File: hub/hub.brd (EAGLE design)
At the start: 31.8 x 25.4 mm, 5 parts

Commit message: closest you can get to Bailey's without getting your nose wet
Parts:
- moved Rπ 2.84 mm to (3.81, 19.1)
- moved C3 1.27 mm to (25.4, 20.3)
- moved XB24 1.27 mm to (7.62, 12.7)
- moved C4 1.27 mm to (27.9, 20.3)
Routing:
- net N$1: track 30.3 -> 29.2 mm
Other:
- board size 31.8 x 25.4 mm -> 29.5 x 26 mm
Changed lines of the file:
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@@
 <board>
 <plain>
-<wire x1="0" y1="0" x2="31.75" y2="0" width="0" layer="20"/>
-<wire x1="31.75" y1="0" x2="31.75" y2="25.4" width="0" layer="20"/>
-<wire x1="31.75" y1="25.4" x2="0" y2="25.4" width="0" layer="20"/>
-<wire x1="0" y1="25.4" x2="0" y2="0" width="0" layer="20"/>
+<wire x1="0" y1="0" x2="29.464" y2="0" width="0" layer="20"/>
+<wire x1="29.464" y1="0" x2="29.464" y2="26.035" width="0" layer="20"/>
+<wire x1="29.464" y1="26.035" x2="0" y2="26.035" width="0" layer="20"/>
+<wire x1="0" y1="26.035" x2="0" y2="0" width="0" layer="20"/>
 <text x="21.59" y="36.83" size="1.778" layer="51" ratio="15">Harold Cooper</text>
 <text x="20.32" y="12.7" size="1.778" layer="21" font="vector" ratio="15" align="center">Heat Seek
@@
 <elements>
 <element name="FRAME1" library="SparkFun-Aesthetics" package="CREATIVE_COMMONS" value="FRAME-LETTER" x="-6.35" y="36.83"/>
-<element name="Rπ" library="SparkFun-Connectors" package="2X5_NOSILK" value="M05X2NO_SILK" x="5.08" y="16.51" rot="MR0"/>
-<element name="XB24" library="hrldcpr" package="XBEE-1" value="XBEE-1XBEE-1" x="8.89" y="12.7" rot="R270"/>
-<element name="C3" library="SparkFun-Capacitors" package="0805" value="1µF" x="26.67" y="20.32" rot="R270"/>
-<element name="C4" library="SparkFun-Capacitors" package="0805" value="8.2pF" x="29.21" y="20.32" rot="R270"/>
+<element name="Rπ" library="SparkFun-Connectors" package="2X5_NOSILK" value="M05X2NO_SILK" x="3.81" y="19.05" rot="MR0"/>
+<element name="XB24" library="hrldcpr" package="XBEE-1" value="XBEE-1XBEE-1" x="7.62" y="12.7" rot="R270"/>
+<element name="C3" library="SparkFun-Capacitors" package="0805" value="1µF" x="25.4" y="20.32" rot="R270"/>
+<element name="C4" library="SparkFun-Capacitors" package="0805" value="8.2pF" x="27.94" y="20.32" rot="R270"/>
 </elements>
 <signals>
@@
 <polygon width="0.3048" layer="1" isolate="0.3048">
 <vertex x="0" y="0"/>
-<vertex x="0" y="25.4"/>
-<vertex x="30.48" y="25.4"/>
-<vertex x="30.48" y="0"/>
+<vertex x="0" y="26.035"/>
+<vertex x="29.464" y="26.035"/>
+<vertex x="29.464" y="0"/>
 </polygon>
 </signal>
@@
 <polygon width="0.3048" layer="16" isolate="0.3048">
 <vertex x="0" y="0"/>
-<vertex x="0" y="25.4"/>
-<vertex x="30.48" y="25.4"/>
-<vertex x="30.48" y="0"/>
+<vertex x="0" y="26.035"/>
+<vertex x="29.464" y="26.035"/>
+<vertex x="29.464" y="0"/>
 </polygon>
 <contactref element="Rπ" pad="1"/>
@@
 <contactref element="C4" pad="1"/>
 <contactref element="XB24" pad="1"/>
-<wire x1="26.67" y1="21.22" x2="29.21" y2="21.22" width="0.254" layer="1"/>
-<wire x1="28.89" y1="23.7" x2="28.89" y2="21.22" width="0.254" layer="1"/>
-<wire x1="28.89" y1="21.22" x2="29.21" y2="21.22" width="0.254" layer="1"/>
+<wire x1="25.4" y1="21.22" x2="27.94" y2="21.22" width="0.254" layer="1"/>
+<wire x1="27.62" y1="23.7" x2="27.62" y2="21.22" width="0.254" layer="1"/>
+<wire x1="27.62" y1="21.22" x2="27.94" y2="21.22" width="0.254" layer="1"/>
 </signal>
 <signal name="N$2">
 <contactref element="Rπ" pad="8"/>
 <contactref element="XB24" pad="3"/>
-<wire x1="3.81" y1="13.97" x2="1.27" y2="11.43" width="0.254" layer="1"/>
-<wire x1="1.27" y1="11.43" x2="3.81" y2="8.89" width="0.254" layer="1"/>
-<wire x1="3.81" y1="8.89" x2="10.08" y2="8.89" width="0.254" layer="1"/>
-<wire x1="10.08" y1="8.89" x2="24.89" y2="23.7" width="0.254" layer="1"/>
+<wire x1="2.54" y1="16.51" x2="1.143" y2="16.51" width="0.254" layer="1"/>
+<wire x1="1.143" y1="16.51" x2="1.143" y2="11.43" width="0.254" layer="1"/>
+<wire x1="23.62" y1="23.7" x2="11.35" y2="11.43" width="0.254" layer="1"/>
+<wire x1="11.35" y1="11.43" x2="1.143" y2="11.43" width="0.254" layer="1"/>
 </signal>
 <signal name="N$1">
 <contactref element="Rπ" pad="10"/>
 <contactref element="XB24" pad="2"/>
-<wire x1="3.81" y1="11.43" x2="6.35" y2="8.89" width="0.254" layer="16"/>
-<wire x1="6.35" y1="8.89" x2="12.08" y2="8.89" width="0.254" layer="16"/>
-<wire x1="12.08" y1="8.89" x2="26.89" y2="23.7" width="0.254" layer="16"/>
+<wire x1="2.54" y1="13.97" x2="5.08" y2="11.43" width="0.254" layer="16"/>
+<wire x1="13.35" y1="11.43" x2="25.62" y2="23.7" width="0.254" layer="16"/>
+<wire x1="5.08" y1="11.43" x2="13.35" y2="11.43" width="0.254" layer="16"/>
 </signal>
 </signals>

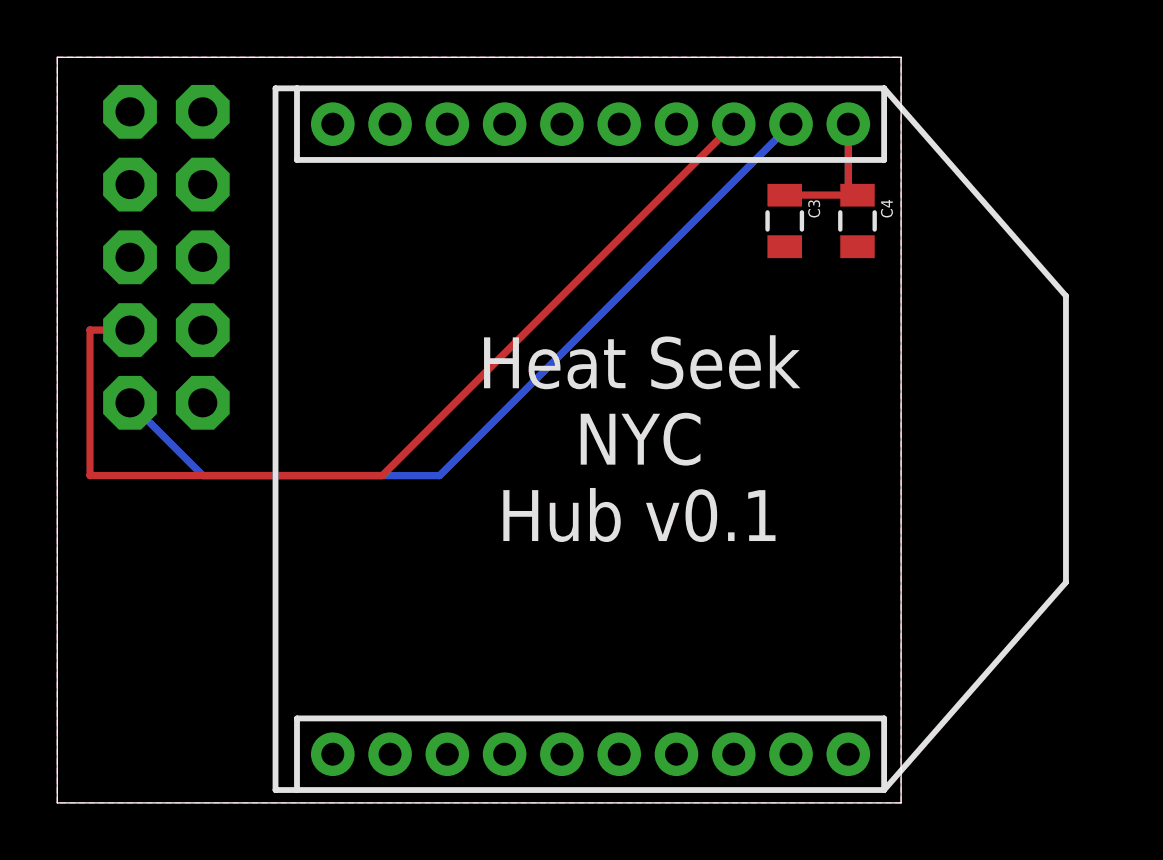
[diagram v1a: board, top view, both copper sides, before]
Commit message: use the largest header we can fit, for stability and to look cool?
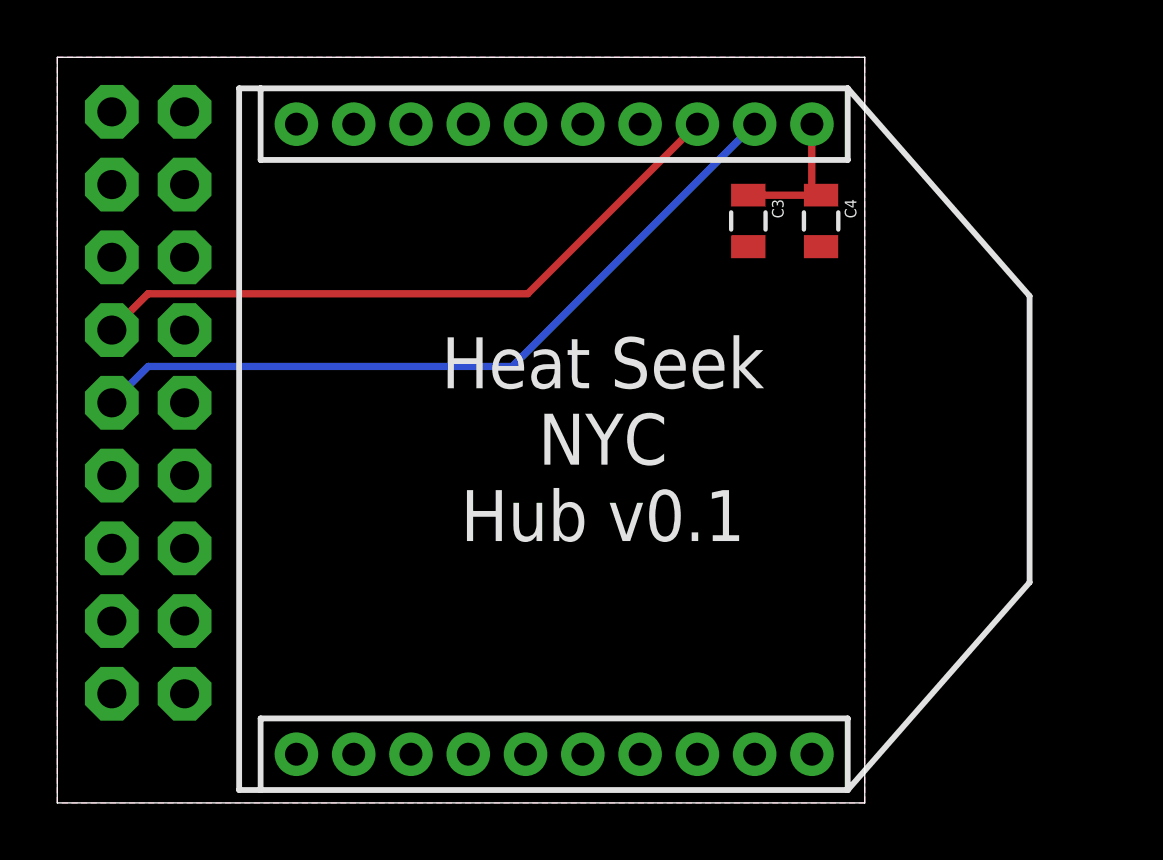
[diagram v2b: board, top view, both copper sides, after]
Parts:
- Rπ: value M05X2NO_SILK -> M9X2; device SparkFun-Connectors:2X5_NOSILK -> hrldcpr:2X9_NOSILK
- moved Rπ 5.12 mm to (3.17, 14.0), turned to 270 degrees
- moved XB24 1.27 mm to (6.35, 12.7)
- moved C3 1.27 mm to (24.1, 20.3)
- moved C4 1.27 mm to (26.7, 20.3)
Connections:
- net 3.3V: now also Rπ.17
- net GND: now also Rπ.14
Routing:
- net N$2: track 34.0 -> 23.4 mm
- net N$1: track 29.2 -> 26.5 mm
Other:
- board size 29.5 x 26 mm -> 28.2 x 26 mm
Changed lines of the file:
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@@
 <board>
 <plain>
-<wire x1="0" y1="0" x2="29.464" y2="0" width="0" layer="20"/>
-<wire x1="29.464" y1="0" x2="29.464" y2="26.035" width="0" layer="20"/>
-<wire x1="29.464" y1="26.035" x2="0" y2="26.035" width="0" layer="20"/>
+<wire x1="0" y1="0" x2="28.194" y2="0" width="0" layer="20"/>
+<wire x1="28.194" y1="0" x2="28.194" y2="26.035" width="0" layer="20"/>
+<wire x1="28.194" y1="26.035" x2="0" y2="26.035" width="0" layer="20"/>
 <wire x1="0" y1="26.035" x2="0" y2="0" width="0" layer="20"/>
 <text x="21.59" y="36.83" size="1.778" layer="51" ratio="15">Harold Cooper</text>
-<text x="20.32" y="12.7" size="1.778" layer="21" font="vector" ratio="15" align="center">Heat Seek
+<text x="19.05" y="12.7" size="1.778" layer="21" font="vector" ratio="15" align="center">Heat Seek
 NYC
 Hub v0.1</text>
@@
 <elements>
 <element name="FRAME1" library="SparkFun-Aesthetics" package="CREATIVE_COMMONS" value="FRAME-LETTER" x="-6.35" y="36.83"/>
-<element name="Rπ" library="SparkFun-Connectors" package="2X5_NOSILK" value="M05X2NO_SILK" x="3.81" y="19.05" rot="MR0"/>
-<element name="XB24" library="hrldcpr" package="XBEE-1" value="XBEE-1XBEE-1" x="7.62" y="12.7" rot="R270"/>
-<element name="C3" library="SparkFun-Capacitors" package="0805" value="1µF" x="25.4" y="20.32" rot="R270"/>
-<element name="C4" library="SparkFun-Capacitors" package="0805" value="8.2pF" x="27.94" y="20.32" rot="R270"/>
+<element name="Rπ" library="hrldcpr" package="2X9_NOSILK" value="M9X2" x="3.175" y="13.97" rot="MR270"/>
+<element name="XB24" library="hrldcpr" package="XBEE-1" value="XBEE-1XBEE-1" x="6.35" y="12.7" rot="R270"/>
+<element name="C3" library="SparkFun-Capacitors" package="0805" value="1µF" x="24.13" y="20.32" rot="R270"/>
+<element name="C4" library="SparkFun-Capacitors" package="0805" value="8.2pF" x="26.67" y="20.32" rot="R270"/>
 </elements>
 <signals>
@@
 <vertex x="0" y="0"/>
 <vertex x="0" y="26.035"/>
-<vertex x="29.464" y="26.035"/>
-<vertex x="29.464" y="0"/>
+<vertex x="28.194" y="26.035"/>
+<vertex x="28.194" y="0"/>
 </polygon>
+<contactref element="Rπ" pad="14"/>
 </signal>
 <signal name="VREF">
@@
 <vertex x="0" y="0"/>
 <vertex x="0" y="26.035"/>
-<vertex x="29.464" y="26.035"/>
-<vertex x="29.464" y="0"/>
+<vertex x="28.194" y="26.035"/>
+<vertex x="28.194" y="0"/>
 </polygon>
 <contactref element="Rπ" pad="1"/>
@@
 <contactref element="C4" pad="1"/>
 <contactref element="XB24" pad="1"/>
-<wire x1="25.4" y1="21.22" x2="27.94" y2="21.22" width="0.254" layer="1"/>
-<wire x1="27.62" y1="23.7" x2="27.62" y2="21.22" width="0.254" layer="1"/>
-<wire x1="27.62" y1="21.22" x2="27.94" y2="21.22" width="0.254" layer="1"/>
+<wire x1="24.13" y1="21.22" x2="26.67" y2="21.22" width="0.254" layer="1"/>
+<wire x1="26.35" y1="23.7" x2="26.35" y2="21.22" width="0.254" layer="1"/>
+<wire x1="26.35" y1="21.22" x2="26.67" y2="21.22" width="0.254" layer="1"/>
+<contactref element="Rπ" pad="17"/>
 </signal>
 <signal name="N$2">
 <contactref element="Rπ" pad="8"/>
 <contactref element="XB24" pad="3"/>
-<wire x1="2.54" y1="16.51" x2="1.143" y2="16.51" width="0.254" layer="1"/>
-<wire x1="1.143" y1="16.51" x2="1.143" y2="11.43" width="0.254" layer="1"/>
-<wire x1="23.62" y1="23.7" x2="11.35" y2="11.43" width="0.254" layer="1"/>
-<wire x1="11.35" y1="11.43" x2="1.143" y2="11.43" width="0.254" layer="1"/>
+<wire x1="1.905" y1="16.51" x2="3.175" y2="17.78" width="0.254" layer="1"/>
+<wire x1="3.175" y1="17.78" x2="16.43" y2="17.78" width="0.254" layer="1"/>
+<wire x1="16.43" y1="17.78" x2="22.35" y2="23.7" width="0.254" layer="1"/>
 </signal>
 <signal name="N$1">
+<contactref element="XB24" pad="2"/>
+<wire x1="3.175" y1="15.24" x2="15.89" y2="15.24" width="0.254" layer="16"/>
+<wire x1="15.89" y1="15.24" x2="24.35" y2="23.7" width="0.254" layer="16"/>
 <contactref element="Rπ" pad="10"/>
-<contactref element="XB24" pad="2"/>
-<wire x1="2.54" y1="13.97" x2="5.08" y2="11.43" width="0.254" layer="16"/>
-<wire x1="13.35" y1="11.43" x2="25.62" y2="23.7" width="0.254" layer="16"/>
-<wire x1="5.08" y1="11.43" x2="13.35" y2="11.43" width="0.254" layer="16"/>
+<wire x1="1.905" y1="13.97" x2="3.175" y2="15.24" width="0.254" layer="16"/>
 </signal>
 </signals>
